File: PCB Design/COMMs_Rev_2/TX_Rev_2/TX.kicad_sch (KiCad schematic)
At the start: 54 parts, among them J1 Conn_01x24_Pin, J2 Conn_01x24_Pin, J3 Conn_01x03_Pin, J4 Conn_01x04_Pin, Q1 IPD50N10S3L16ATMA1, Q2 IPD50N10S3L16ATMA1, Q3 IPD50N10S3L16ATMA1, Q4 IPD50N10S3L16ATMA1, U1 UCC27211AQDDARQ1, U2 UCC27211AQDDARQ1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

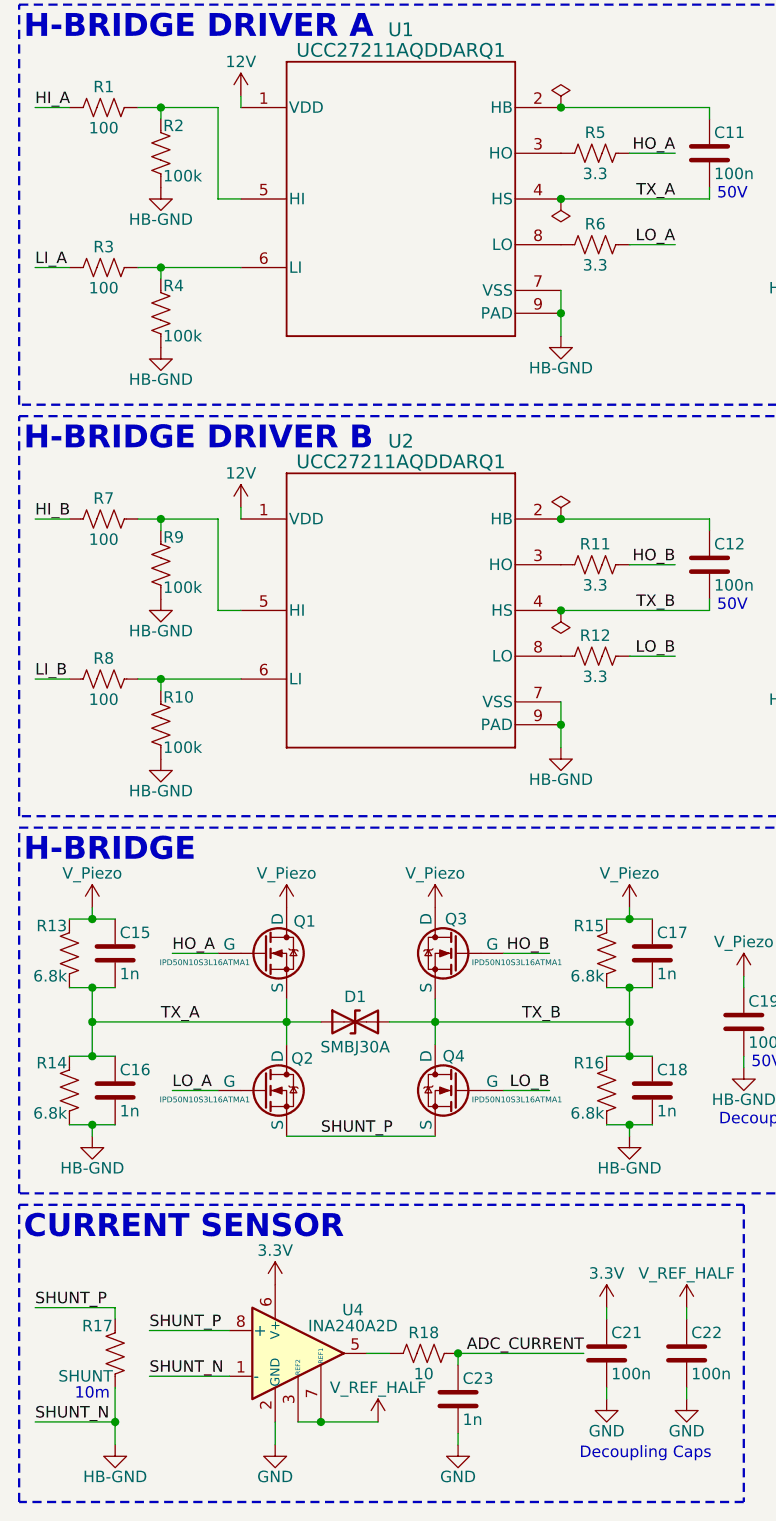
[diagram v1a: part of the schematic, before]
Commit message: Update TX.kicad_sch
R5, R6, R11, R12: 3.3Ω → 10Ω (gate resistors)
R17: SHUNT → 0.01 (10mΩ shunt, 2512 footprint already correct)
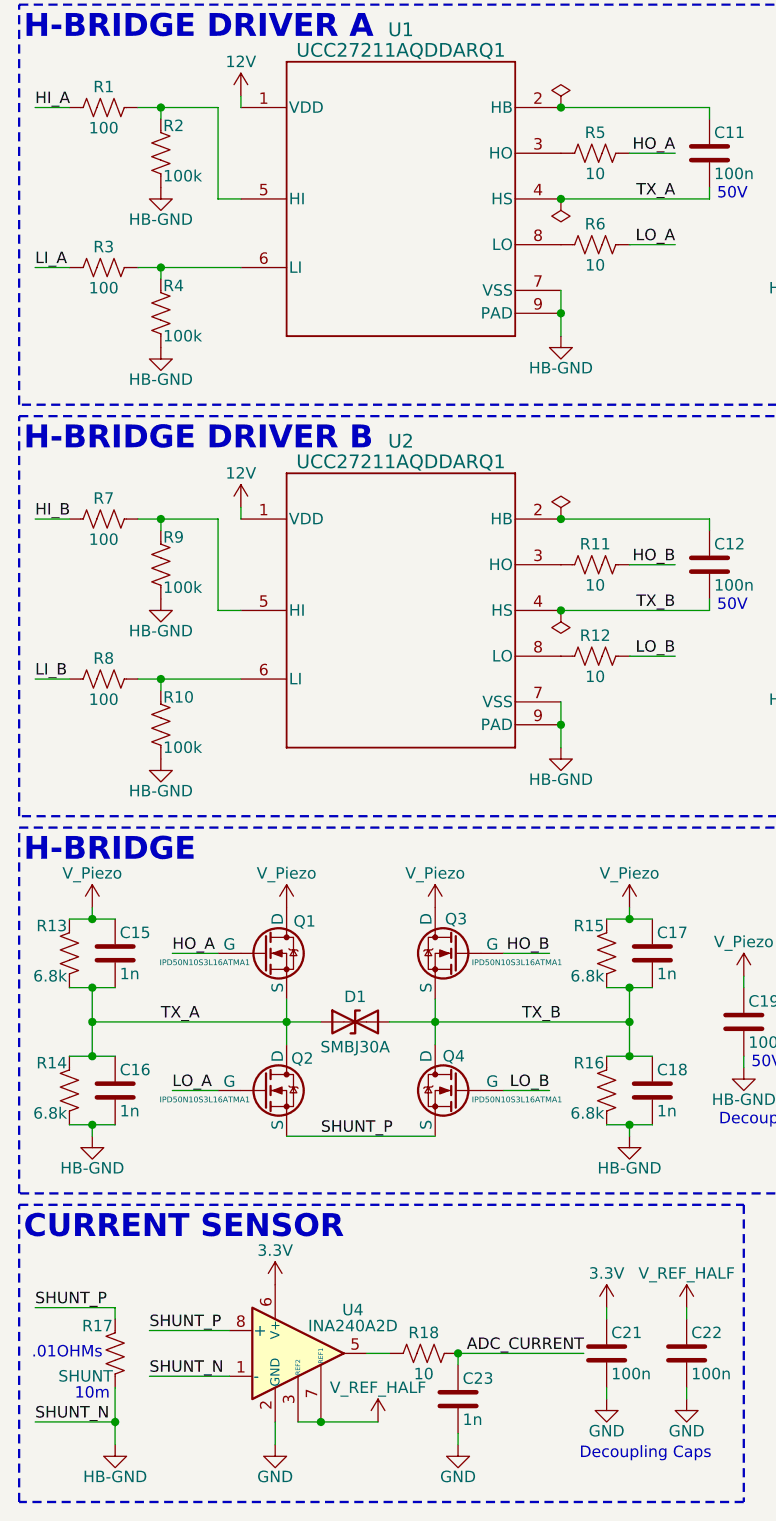
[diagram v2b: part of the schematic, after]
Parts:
- R11, R12, R5, R6: value 3.3 -> 10
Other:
- note added: ".01OHMs"
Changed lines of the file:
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@@
 		)
 	)
+	(text ".01OHMs"
+		(exclude_from_sim no)
+		(at 18.796 163.83 0)
+		(effects
+			(font
+				(size 1.27 1.27)
+			)
+		)
+	)
 	(text "Decoupling Caps"
 		(exclude_from_sim no)
@@
 	)
 	(symbol
+		(lib_id "Device:R_US")
+		(at 77.47 76.2 90)
+		(unit 1)
+		(exclude_from_sim no)
+		(in_bom yes)
+		(on_board yes)
+		(dnp no)
+		(property "Reference" "R11"
+			(at 77.47 73.914 90)
+			(effects
+				(font
+					(size 1.27 1.27)
+				)
+			)
+		)
+		(property "Value" "10"
+			(at 77.47 78.486 90)
+			(effects
+				(font
+					(size 1.27 1.27)
+				)
+			)
+		)
+		(property "Footprint" "Resistor_SMD:R_0603_1608Metric"
+			(at 77.724 75.184 90)
+			(effects
+				(font
+					(size 1.27 1.27)
+				)
+				(hide yes)
+			)
+		)
+		(property "Datasheet" "~"
+			(at 77.47 76.2 0)
+			(effects
+				(font
+					(size 1.27 1.27)
+				)
+				(hide yes)
+			)
+		)
+		(property "Description" "Resistor, US symbol"
+			(at 77.47 76.2 0)
+			(effects
+				(font
+					(size 1.27 1.27)
+				)
+				(hide yes)
+			)
+		)
+		(pin "2"
+		)
+		(pin "1"
+		)
+		(instances
+			(project "TX"
+				(path "/db628952-7712-4c33-95ca-df895d26f0e8"
+					(reference "R11")
+					(unit 1)
+				)
+			)
+		)
+	)
+	(symbol
 		(lib_id "power:GND")
 		(at 204.47 34.29 0)
@@
 	)
 	(symbol
-		(lib_id "Device:R_US")
-		(at 77.47 40.64 90)
-		(unit 1)
-		(exclude_from_sim no)
-		(in_bom yes)
-		(on_board yes)
-		(dnp no)
-		(property "Reference" "R6"
-			(at 77.47 38.354 90)
-			(effects
-				(font
-					(size 1.27 1.27)
-				)
-			)
-		)
-		(property "Value" "3.3"
-			(at 77.47 42.926 90)
-			(effects
-				(font
-					(size 1.27 1.27)
-				)
-			)
-		)
-		(property "Footprint" "Resistor_SMD:R_0603_1608Metric"
-			(at 77.724 39.624 90)
-			(effects
-				(font
-					(size 1.27 1.27)
-				)
-				(hide yes)
-			)
-		)
-		(property "Datasheet" "~"
-			(at 77.47 40.64 0)
-			(effects
-				(font
-					(size 1.27 1.27)
-				)
-				(hide yes)
-			)
-		)
-		(property "Description" "Resistor, US symbol"
-			(at 77.47 40.64 0)
-			(effects
-				(font
-					(size 1.27 1.27)
-				)
-				(hide yes)
-			)
-		)
-		(pin "2"
-		)
-		(pin "1"
-		)
-		(instances
-			(project "TX"
-				(path "/db628952-7712-4c33-95ca-df895d26f0e8"
-					(reference "R6")
-					(unit 1)
-				)
-			)
-		)
-	)
-	(symbol
 		(lib_id "power:VCC")
 		(at 127 27.94 270)
@@
 	)
 	(symbol
+		(lib_id "Device:R_US")
+		(at 77.47 86.36 90)
+		(unit 1)
+		(exclude_from_sim no)
+		(in_bom yes)
+		(on_board yes)
+		(dnp no)
+		(property "Reference" "R12"
+			(at 77.47 84.074 90)
+			(effects
+				(font
+					(size 1.27 1.27)
+				)
+			)
+		)
+		(property "Value" "10"
+			(at 77.47 88.646 90)
+			(effects
+				(font
+					(size 1.27 1.27)
+				)
+			)
+		)
+		(property "Footprint" "Resistor_SMD:R_0603_1608Metric"
+			(at 77.724 85.344 90)
+			(effects
+				(font
+					(size 1.27 1.27)
+				)
+				(hide yes)
+			)
+		)
+		(property "Datasheet" "~"
+			(at 77.47 86.36 0)
+			(effects
+				(font
+					(size 1.27 1.27)
+				)
+				(hide yes)
+			)
+		)
+		(property "Description" "Resistor, US symbol"
+			(at 77.47 86.36 0)
+			(effects
+				(font
+					(size 1.27 1.27)
+				)
+				(hide yes)
+			)
+		)
+		(pin "2"
+		)
+		(pin "1"
+		)
+		(instances
+			(project "TX"
+				(path "/db628952-7712-4c33-95ca-df895d26f0e8"
+					(reference "R12")
+					(unit 1)
+				)
+			)
+		)
+	)
+	(symbol
 		(lib_id "Device:C")
 		(at 195.58 29.21 0)
@@
 	)
 	(symbol
-		(lib_id "Device:R_US")
-		(at 77.47 86.36 90)
-		(unit 1)
-		(exclude_from_sim no)
-		(in_bom yes)
-		(on_board yes)
-		(dnp no)
-		(property "Reference" "R12"
-			(at 77.47 84.074 90)
-			(effects
-				(font
-					(size 1.27 1.27)
-				)
-			)
-		)
-		(property "Value" "3.3"
-			(at 77.47 88.646 90)
-			(effects
-				(font
-					(size 1.27 1.27)
-				)
-			)
-		)
-		(property "Footprint" "Resistor_SMD:R_0603_1608Metric"
-			(at 77.724 85.344 90)
-			(effects
-				(font
-					(size 1.27 1.27)
-				)
-				(hide yes)
-			)
-		)
-		(property "Datasheet" "~"
-			(at 77.47 86.36 0)
-			(effects
-				(font
-					(size 1.27 1.27)
-				)
-				(hide yes)
-			)
-		)
-		(property "Description" "Resistor, US symbol"
-			(at 77.47 86.36 0)
-			(effects
-				(font
-					(size 1.27 1.27)
-				)
-				(hide yes)
-			)
-		)
-		(pin "2"
-		)
-		(pin "1"
-		)
-		(instances
-			(project "TX"
-				(path "/db628952-7712-4c33-95ca-df895d26f0e8"
-					(reference "R12")
-					(unit 1)
-				)
-			)
-		)
-	)
-	(symbol
 		(lib_id "power:GND")
 		(at 177.8 63.5 0)
@@
 	)
 	(symbol
-		(lib_id "Device:R_US")
-		(at 77.47 76.2 90)
-		(unit 1)
-		(exclude_from_sim no)
-		(in_bom yes)
-		(on_board yes)
-		(dnp no)
-		(property "Reference" "R11"
-			(at 77.47 73.914 90)
-			(effects
-				(font
-					(size 1.27 1.27)
-				)
-			)
-		)
-		(property "Value" "3.3"
-			(at 77.47 78.486 90)
-			(effects
-				(font
-					(size 1.27 1.27)
-				)
-			)
-		)
-		(property "Footprint" "Resistor_SMD:R_0603_1608Metric"
-			(at 77.724 75.184 90)
-			(effects
-				(font
-					(size 1.27 1.27)
-				)
-				(hide yes)
-			)
-		)
-		(property "Datasheet" "~"
-			(at 77.47 76.2 0)
-			(effects
-				(font
-					(size 1.27 1.27)
-				)
-				(hide yes)
-			)
-		)
-		(property "Description" "Resistor, US symbol"
-			(at 77.47 76.2 0)
-			(effects
-				(font
-					(size 1.27 1.27)
-				)
-				(hide yes)
-			)
-		)
-		(pin "2"
-		)
-		(pin "1"
-		)
-		(instances
-			(project "TX"
-				(path "/db628952-7712-4c33-95ca-df895d26f0e8"
-					(reference "R11")
-					(unit 1)
-				)
-			)
-		)
-	)
-	(symbol
 		(lib_id "power:GND")
 		(at 195.58 63.5 0)
@@
 	)
 	(symbol
+		(lib_id "Device:R_US")
+		(at 77.47 40.64 90)
+		(unit 1)
+		(exclude_from_sim no)
+		(in_bom yes)
+		(on_board yes)
+		(dnp no)
+		(property "Reference" "R6"
+			(at 77.47 38.354 90)
+			(effects
+				(font
+					(size 1.27 1.27)
+				)
+			)
+		)
+		(property "Value" "10"
+			(at 77.47 42.926 90)
+			(effects
+				(font
+					(size 1.27 1.27)
+				)
+			)
+		)
+		(property "Footprint" "Resistor_SMD:R_0603_1608Metric"
+			(at 77.724 39.624 90)
+			(effects
+				(font
+					(size 1.27 1.27)
+				)
+				(hide yes)
+			)
+		)
+		(property "Datasheet" "~"
+			(at 77.47 40.64 0)
+			(effects
+				(font
+					(size 1.27 1.27)
+				)
+				(hide yes)
+			)
+		)
+		(property "Description" "Resistor, US symbol"
+			(at 77.47 40.64 0)
+			(effects
+				(font
+					(size 1.27 1.27)
+				)
+				(hide yes)
+			)
+		)
+		(pin "2"
+		)
+		(pin "1"
+		)
+		(instances
+			(project "TX"
+				(path "/db628952-7712-4c33-95ca-df895d26f0e8"
+					(reference "R6")
+					(unit 1)
+				)
+			)
+		)
+	)
+	(symbol
 		(lib_id "power:GND")
 		(at 41.91 173.99 0)
@@
 			)
 		)
-		(property "Value" "3.3"
+		(property "Value" "10"
 			(at 77.47 32.766 90)
 			(effects

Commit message: Added PWR Export Files
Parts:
- removed D1: SMBJ30A, Diode_SMD:D_SMB, symbol Device:D_TVS
- added L1, L2: L, symbol Device:L
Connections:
- net TX_A: now also L1.2; no longer C15.2, C16.1, Q1.3 (S), Q2.1 (D), R13.2, R14.1
- net TX_B: now also L2.2; no longer C17.2, C18.1, Q3.3 (S), Q4.1 (D), R15.2, R16.1
- new net H_A: C15.2, C16.1, L1.1, Q1.3 (S), Q2.1 (D), R13.2, R14.1
- new net H_B: C17.2, C18.1, L2.1, Q3.3 (S), Q4.1 (D), R15.2, R16.1
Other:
- note added: "IMPEDANCE MATCHING"
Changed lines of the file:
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@@
 		)
 	)
+	(rectangle
+		(start 111.76 105.41)
+		(end 154.94 123.19)
+		(stroke
+			(width 0.254)
+			(type dash_dot)
+		)
+		(fill
+			(type none)
+		)
+	)
 	(text "50V"
 		(exclude_from_sim no)
@@
 		)
 	)
+	(text "IMPEDANCE MATCHING"
+		(exclude_from_sim no)
+		(at 112.268 107.95 0)
+		(effects
+			(font
+				(size 2.54 2.54)
+				(thickness 0.254)
+				(bold yes)
+			)
+			(justify left)
+		)
+	)
 	(text "BULK DECOUPLING"
 		(exclude_from_sim no)
@@
 	(wire
 		(pts
-			(xy 43.18 127) (xy 46.99 127)
-		)
-		(stroke
-			(width 0)
-			(type default)
-		)
-	)
-	(wire
-		(pts
 			(xy 26.67 88.9) (xy 29.21 88.9)
 		)
@@
 	(wire
 		(pts
-			(xy 54.61 127) (xy 59.69 127)
-		)
-		(stroke
-			(width 0)
-			(type default)
-		)
-	)
-	(wire
-		(pts
 			(xy 15.24 71.12) (xy 19.05 71.12)
 		)
@@
 	(wire
 		(pts
+			(xy 135.89 113.03) (xy 143.51 113.03)
+		)
+		(stroke
+			(width 0)
+			(type default)
+		)
+	)
+	(wire
+		(pts
 			(xy 109.22 86.36) (xy 109.22 87.63)
 		)
@@
 	(wire
 		(pts
+			(xy 121.92 119.38) (xy 128.27 119.38)
+		)
+		(stroke
+			(width 0)
+			(type default)
+		)
+	)
+	(wire
+		(pts
 			(xy 90.17 35.56) (xy 90.17 34.29)
 		)
@@
 	(wire
 		(pts
+			(xy 121.92 113.03) (xy 128.27 113.03)
+		)
+		(stroke
+			(width 0)
+			(type default)
+		)
+	)
+	(wire
+		(pts
 			(xy 35.56 25.4) (xy 35.56 35.56)
 		)
@@
 	(wire
 		(pts
+			(xy 135.89 119.38) (xy 143.51 119.38)
+		)
+		(stroke
+			(width 0)
+			(type default)
+		)
+	)
+	(wire
+		(pts
 			(xy 102.87 130.81) (xy 102.87 132.08)
 		)
@@
 		)
 	)
-	(label "TX_B"
-		(at 73.66 127 180)
+	(label "H_B"
+		(at 64.77 127 180)
 		(effects
 			(font
@@
 		)
 	)
+	(label "H_B"
+		(at 121.92 119.38 0)
+		(effects
+			(font
+				(size 1.27 1.27)
+			)
+			(justify left bottom)
+		)
+	)
 	(label "SHUNT_P"
 		(at 46.99 139.7 0)
@@
 		)
 	)
+	(label "TX_B"
+		(at 143.51 119.38 180)
+		(effects
+			(font
+				(size 1.27 1.27)
+			)
+			(justify right bottom)
+		)
+	)
 	(label "LO_A"
 		(at 30.48 134.62 0)
@@
 		)
 	)
-	(label "TX_A"
-		(at 29.21 127 0)
+	(label "H_A"
+		(at 38.1 127 0)
 		(effects
 			(font
@@
 		)
 	)
+	(label "H_A"
+		(at 121.92 113.03 0)
+		(effects
+			(font
+				(size 1.27 1.27)
+			)
+			(justify left bottom)
+		)
+	)
 	(label "ADC_CURRENT"
 		(at 76.2 163.83 180)
@@
 		)
 	)
+	(label "TX_A"
+		(at 143.51 113.03 180)
+		(effects
+			(font
+				(size 1.27 1.27)
+			)
+			(justify right bottom)
+		)
+	)
 	(label "HI_A"
 		(at 15.24 25.4 0)
@@
 	)
 	(symbol
-		(lib_id "Device:D_TVS")
-		(at 50.8 127 0)
-		(unit 1)
-		(exclude_from_sim no)
-		(in_bom yes)
-		(on_board yes)
-		(dnp no)
-		(property "Reference" "D1"
-			(at 50.8 124.206 0)
-			(effects
-				(font
-					(size 1.27 1.27)
-				)
-			)
-		)
-		(property "Value" "SMBJ30A"
-			(at 50.8 129.794 0)
-			(effects
-				(font
-					(size 1.27 1.27)
-				)
-			)
-		)
-		(property "Footprint" "Diode_SMD:D_SMB"
-			(at 50.8 127 0)
-			(effects
-				(font
-					(size 1.27 1.27)
-				)
-				(hide yes)
-			)
-		)
-		(property "Datasheet" "~"
-			(at 50.8 127 0)
-			(effects
-				(font
-					(size 1.27 1.27)
-				)
-				(hide yes)
-			)
-		)
-		(property "Description" "Bidirectional transient-voltage-suppression diode"
-			(at 50.8 127 0)
-			(effects
-				(font
-					(size 1.27 1.27)
-				)
-				(hide yes)
-			)
-		)
-		(pin "1"
-		)
-		(pin "2"
-		)
-		(instances
-			(project ""
-				(path "/db628952-7712-4c33-95ca-df895d26f0e8"
-					(reference "D1")
-					(unit 1)
-				)
-			)
-		)
-	)
-	(symbol
 		(lib_id "power:VCC")
 		(at 109.22 77.47 0)
@@
 	)
 	(symbol
+		(lib_id "Device:L")
+		(at 132.08 113.03 90)
+		(unit 1)
+		(exclude_from_sim no)
+		(in_bom yes)
+		(on_board yes)
+		(dnp no)
+		(property "Reference" "L1"
+			(at 132.08 111.252 90)
+			(effects
+				(font
+					(size 1.27 1.27)
+				)
+			)
+		)
+		(property "Value" "L"
+			(at 132.08 114.3 90)
+			(effects
+				(font
+					(size 1.27 1.27)
+				)
+			)
+		)
+		(property "Footprint" ""
+			(at 132.08 113.03 0)
+			(effects
+				(font
+					(size 1.27 1.27)
+				)
+				(hide yes)
+			)
+		)
+		(property "Datasheet" "~"
+			(at 132.08 113.03 0)
+			(effects
+				(font
+					(size 1.27 1.27)
+				)
+				(hide yes)
+			)
+		)
+		(property "Description" "Inductor"
+			(at 132.08 113.03 0)
+			(effects
+				(font
+					(size 1.27 1.27)
+				)
+				(hide yes)
+			)
+		)
+		(pin "1"
+		)
+		(pin "2"
+		)
+		(instances
+			(project ""
+				(path "/db628952-7712-4c33-95ca-df895d26f0e8"
+					(reference "L1")
+					(unit 1)
+				)
+			)
+		)
+	)
+	(symbol
 		(lib_id "power:GND")
 		(at 195.58 63.5 0)
@@
 					(unit 1)
 				)
+			)
+		)
+	)
+	(symbol
+		(lib_id "Device:L")
+		(at 132.08 119.38 90)
+		(unit 1)
+		(exclude_from_sim no)
+		(in_bom yes)
+		(on_board yes)
+		(dnp no)
+		(property "Reference" "L2"
+			(at 132.08 117.602 90)
+			(effects
+				(font
+					(size 1.27 1.27)
+				)
+			)
+		)
+		(property "Value" "L"
+			(at 132.08 120.65 90)
+			(effects
+				(font
+					(size 1.27 1.27)
+				)
+			)
+		)
+		(property "Footprint" ""
+			(at 132.08 119.38 0)
+			(effects
+				(font
+					(size 1.27 1.27)
+				)
+				(hide yes)
+			)
+		)
+		(property "Datasheet" "~"
+			(at 132.08 119.38 0)
+			(effects
+				(font
+					(size 1.27 1.27)
+				)
+				(hide yes)
+			)
+		)
+		(property "Description" "Inductor"
+			(at 132.08 119.38 0)
+			(effects
+				(font
+					(size 1.27 1.27)
+				)
+				(hide yes)
+			)
+		)
+		(pin "1"
+		)
+		(pin "2"
+		)
+		(instances
+			(project "TX"
+				(path "/db628952-7712-4c33-95ca-df895d26f0e8"
+					(reference "L2")
+					(unit 1)
+				)

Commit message: Updated Revision Number and Title Block
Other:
- company: (none) -> Capstone
- title: (none) -> SWARM TX COMMs
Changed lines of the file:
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@@
 	(generator_version "9.0")
 	(paper "A4")
+	(title_block
+		(title "SWARM TX COMMs")
+		(date "2026-03-23")
+		(rev "2.1")
+		(company "Capstone")
+		(comment 1 "By SAMANTHA CHONG")
+	)
 	(rectangle
 		(start 13.462 147.32)

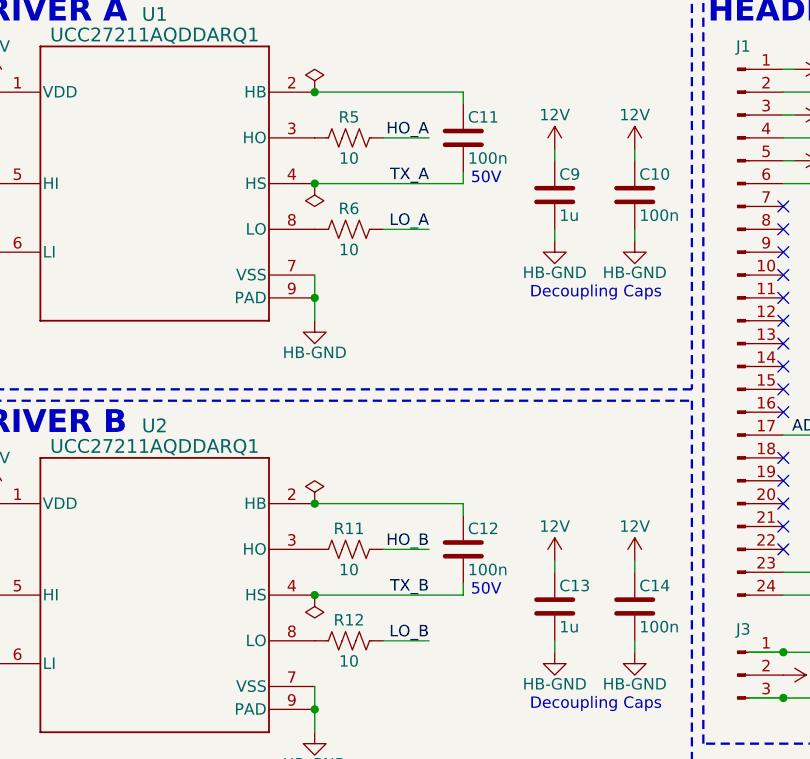
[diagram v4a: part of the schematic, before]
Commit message: Updated Schematic to include Inductor Matching Inductors
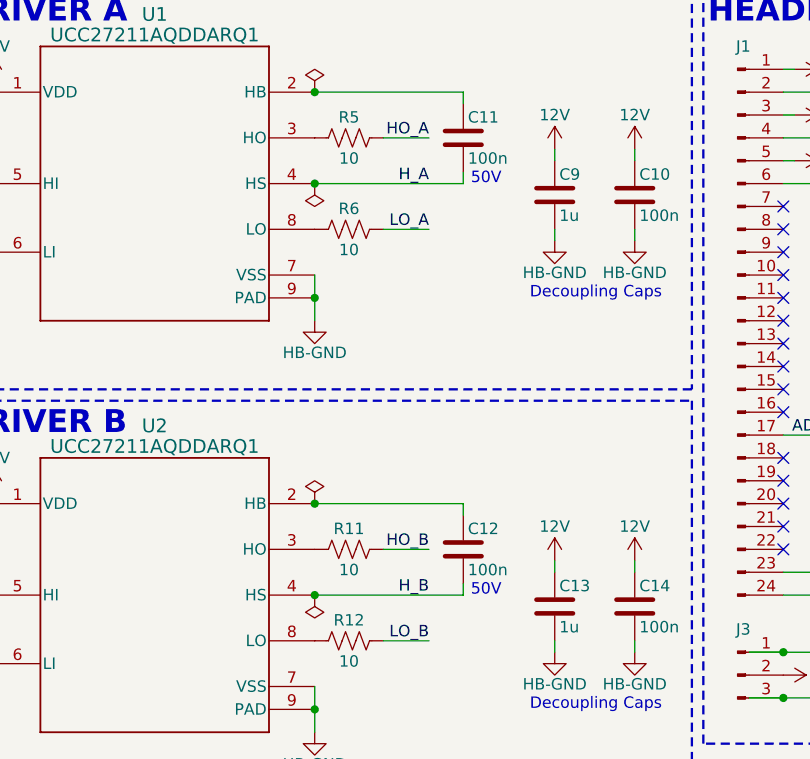
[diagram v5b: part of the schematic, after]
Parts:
- L1, L2: footprint (none) -> Inductor_SMD:L_Wuerth_MAPI-5030
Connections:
- net H_A: now also C11.2, U1.4 (HS)
- net H_B: now also C12.2, U2.4 (HS)
- net TX_A: no longer C11.2, U1.4 (HS)
- net TX_B: no longer C12.2, U2.4 (HS)
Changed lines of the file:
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@@
 		)
 	)
-	(label "TX_A"
+	(label "H_A"
 		(at 86.36 35.56 180)
 		(effects
@@
 		)
 	)
-	(label "TX_B"
+	(label "H_B"
 		(at 86.36 81.28 180)
 		(effects
@@
 			)
 		)
-		(property "Footprint" ""
+		(property "Footprint" "Inductor_SMD:L_Wuerth_MAPI-5030"
 			(at 132.08 113.03 0)
 			(effects
@@
 			)
 		)
-		(property "Footprint" ""
+		(property "Footprint" "Inductor_SMD:L_Wuerth_MAPI-5030"
 			(at 132.08 119.38 0)
 			(effects
